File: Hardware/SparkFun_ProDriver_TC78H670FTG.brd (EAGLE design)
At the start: 50.8 x 57.1 mm, 87 parts, among them J2 LATCH, J3 PTH, J4 LATCH, J5 LATCH, J6 PTH, J7 LATCH, J8 PTH, U1 TC78H670FTG

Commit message: layout almost done still need to add bstop for heatsink
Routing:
- net MODE3: track 0.00 -> 91.9 mm
- net 3.3V: track 0.00 -> 79.0 mm, vias 0 -> 8
- net MODE2: track 0.00 -> 78.8 mm
- net EN: track 0.00 -> 71.6 mm
- net MODE1: track 0.00 -> 67.8 mm
- net MODE0: track 0.00 -> 59.2 mm
- net STBY: track 0.00 -> 47.6 mm
- net VREF: track 0.00 -> 45.1 mm, vias 0 -> 2
- net VM: track 1.21 -> 24.9 mm
- net OSCM: track 0.00 -> 8.56 mm
- net N$1: track 0.00 -> 6.17 mm
- net N$4: track 0.00 -> 6.02 mm
- net N$2: track 0.00 -> 1.98 mm
- net N$5: track 0.00 -> 1.79 mm
- added copper zone on layer 2, net GND
- added copper zone on layer 1, net OUT_A+
- added copper zone on layer 1, net OUT_A-
- added copper zone on layer 1, net OUT_B+
- added copper zone on layer 1, net OUT_B-
- removed copper zone on layer 2, net VM

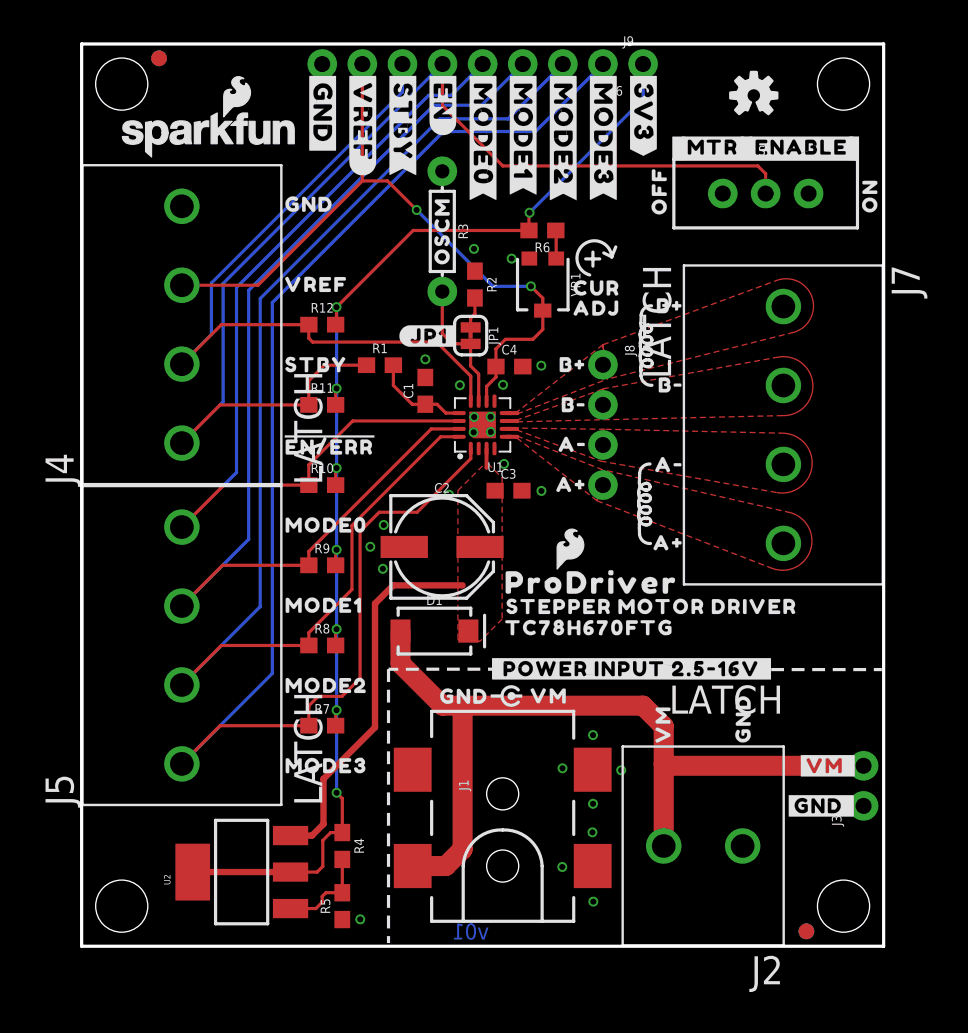
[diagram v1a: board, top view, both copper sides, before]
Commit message: nudged OSCM res away, added bstop for heatsink
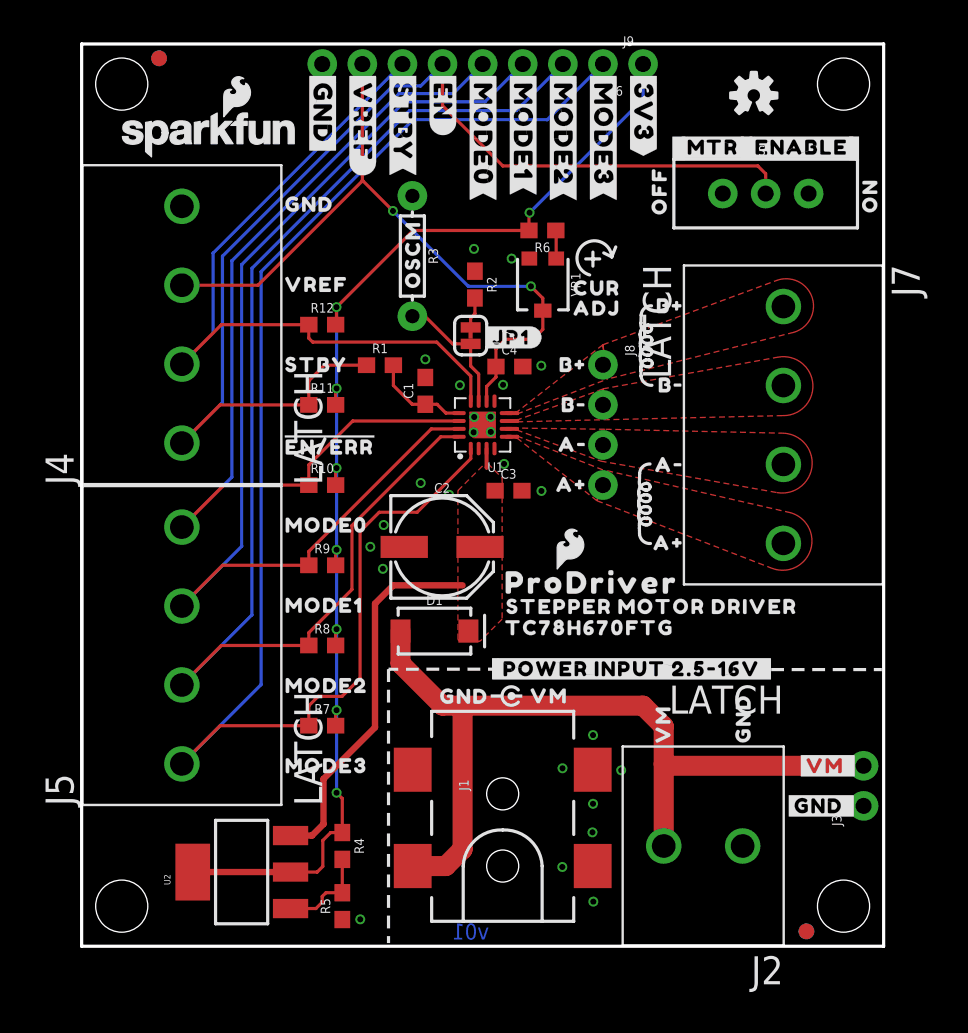
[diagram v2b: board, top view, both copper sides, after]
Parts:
- removed U$13: (no value), output:#JP1#0
- added U$45: (no value), output:#JP1#0
- moved R3 2.45 mm to (20.9, 43.7)
- moved U$18 2.39 mm to (21.0, 41.0)
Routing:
- net MODE3: track 91.9 -> 93.5 mm
- net MODE2: track 78.8 -> 80.2 mm
- net MODE1: track 67.8 -> 69.0 mm
- net MODE0: track 59.2 -> 60.3 mm
- net EN: track 71.6 -> 72.7 mm

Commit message: Corrected EN/ERR pin access
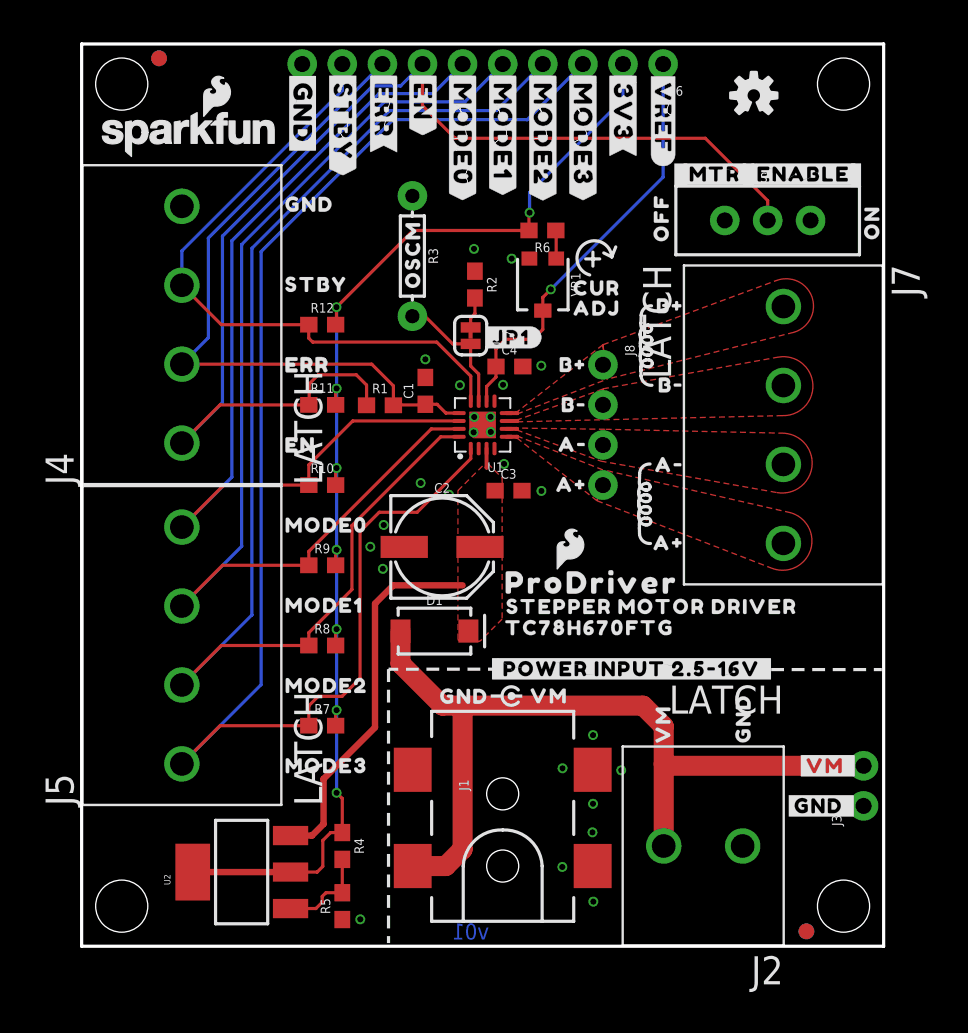
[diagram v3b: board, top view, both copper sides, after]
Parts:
- removed J9: (no value), SparkFun-Connectors:1X01_NO_SILK
- removed U$37: (no value), output:#MODE2#0
- removed U$38: (no value), output:#MODE3#0
- removed U$39: (no value), output:#3V3#0
- added U$13: (no value), output:#EN#2
- added U$46: (no value), output:#MODE1#4
- added U$47: (no value), output:#MODE2#4
- added U$48: (no value), output:#MODE3#4
- J6: device SparkFun-Connectors:1X08_NO_SILK -> SparkFun-Connectors:1X10_NO_SILK
- U$19: device output:#EN#ERR#0 -> output:EN0
- U$33: device output:#STBY#0 -> output:#MODE0#4
- U$34: device output:#EN#0 -> output:#STBY#3
- U$35: device output:#MODE0#0 -> output:#3V3#4
- U$36: device output:#MODE1#0 -> output:ERR4
- U$7: device output:VREF7 -> output:#ERR#7
- moved U$36 24.5 mm to (12.2, 36.8), turned to 0 degrees
- moved U$32 19.0 mm to (36.8, 55.5)
- moved U$7 15.3 mm to (19.1, 55.5), turned to 270 degrees
- moved U$35 8.86 mm to (34.3, 55.5)
- moved U$34 6.35 mm to (16.5, 55.5)
- moved U$8 5.08 mm to (12.2, 41.9)
- moved J6 3.81 mm to (36.8, 55.9)
- moved U$33 3.78 mm to (24.1, 55.5)
- moved R1 2.54 mm to (18.9, 34.3)
- moved S1 1.71 mm to (43.5, 46.0)
- moved U$17 1.71 mm to (36.7, 43.9)
- moved U$14 1.71 mm to (37.8, 48.9)
- moved U$16 1.71 mm to (50.1, 44.1)
- moved U$21 1.71 mm to (42.1, 48.9)
- moved LOGO1 1.27 mm to (6.84, 51.4)
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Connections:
- removed net N$1: C1.1, R1.2, U1.13
- new net ERR: C1.1, J4.2, J6.8, R1.2, U1.13
- net 3.3V: now also J6.2; no longer J9.1
- net EN: now also J6.7; no longer J6.5
- net GND: now also J6.10; no longer J6.8
- net MODE0: now also J6.6; no longer J6.4
- net MODE1: now also J6.5; no longer J6.3
- net MODE2: now also J6.4; no longer J6.2
- net MODE3: now also J6.3; no longer J6.1
- net STBY: now also J4.3, J6.9; no longer J4.2, J6.6
- net VREF: now also J6.1; no longer J4.3, J6.7
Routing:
- net ERR: track 0.00 -> 44.0 mm
- net VREF: track 45.1 -> 27.0 mm, vias 2 -> 1
- net STBY: track 47.6 -> 41.0 mm
- net N$1: track 6.17 -> 0.00 mm
- net EN: track 72.7 -> 75.5 mm
- net MODE3: track 93.5 -> 93.0 mm
- net MODE2: track 80.2 -> 79.7 mm
- net 3.3V: track 79.0 -> 78.5 mm
- net MODE1: track 69.0 -> 68.5 mm
- net MODE0: track 60.3 -> 59.8 mm

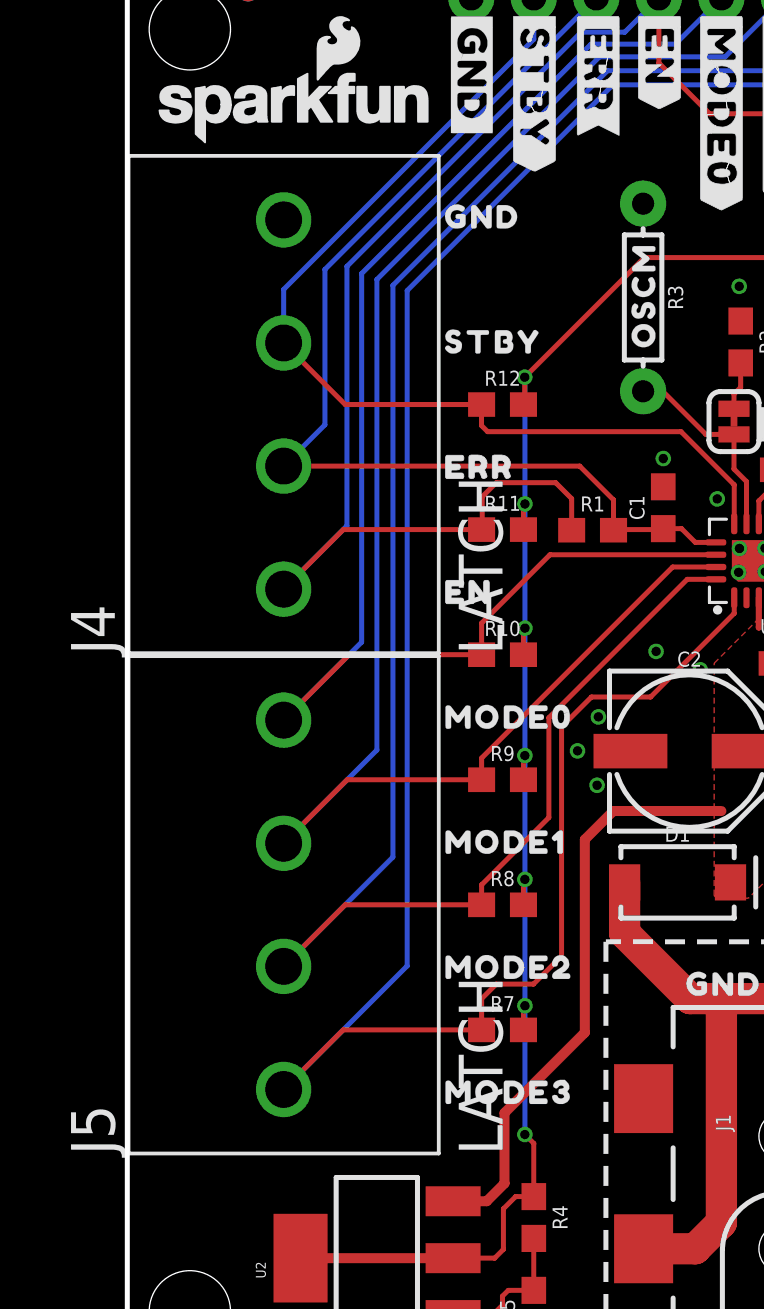
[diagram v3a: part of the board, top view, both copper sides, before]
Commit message: nudged 1x4 latch terminals apart to avoid part collision
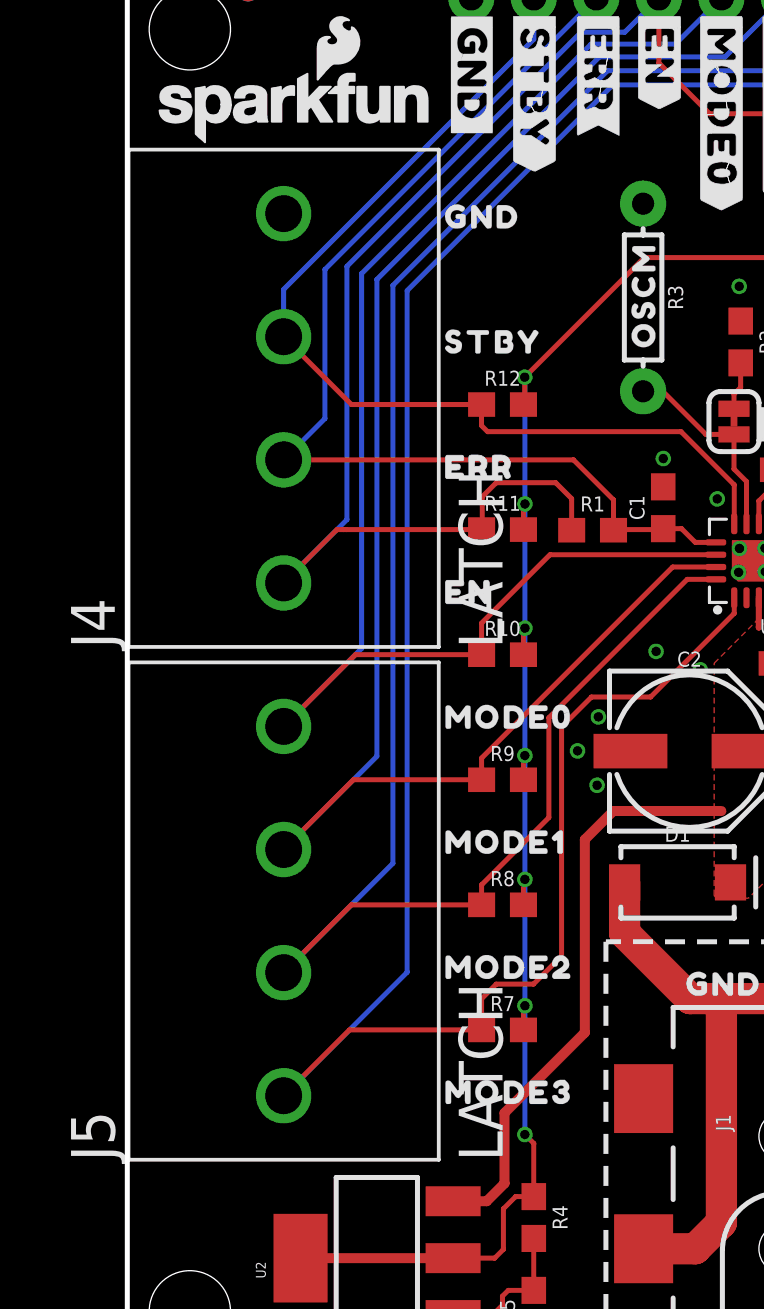
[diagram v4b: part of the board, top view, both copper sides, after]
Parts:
- moved J4 0.25 mm to (6.35, 39.6)
- moved J5 0.25 mm to (6.35, 18.8)

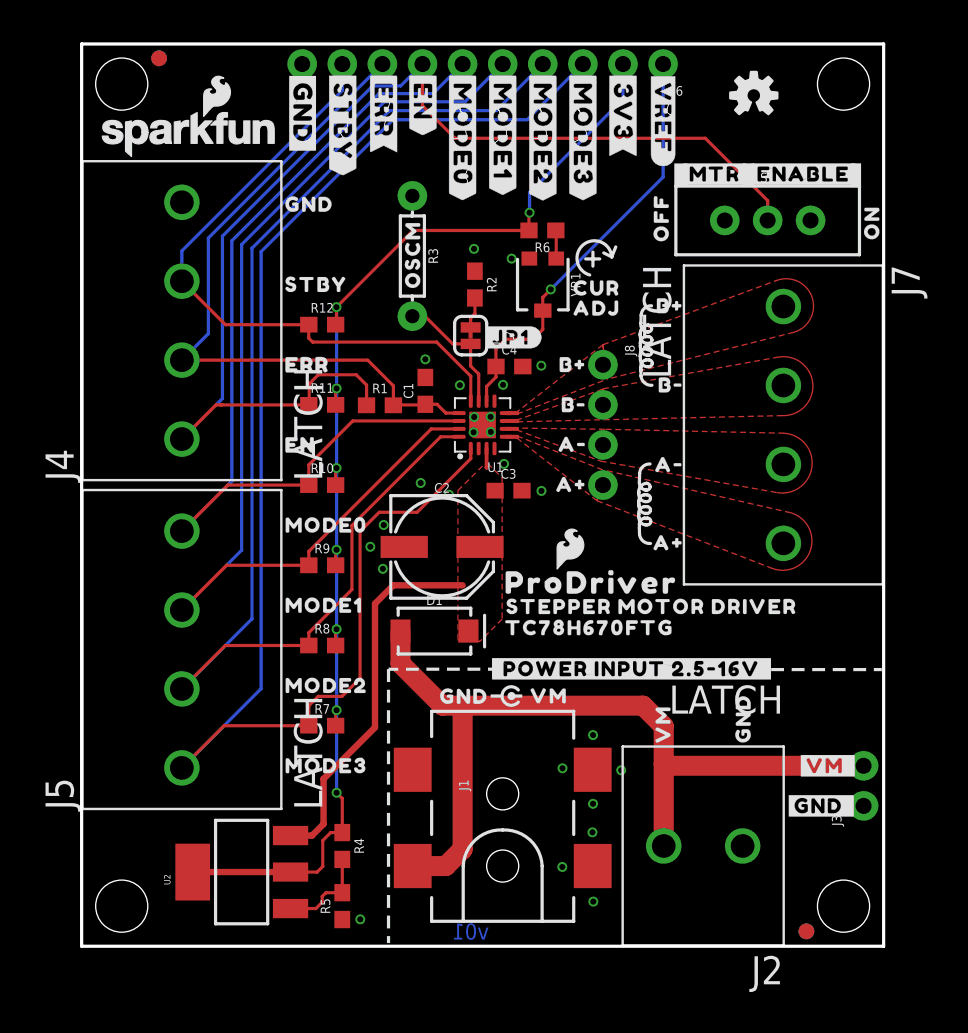
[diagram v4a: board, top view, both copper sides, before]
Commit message: moved connectors inward to allow for depanel blade space
Also added tcream to IC package
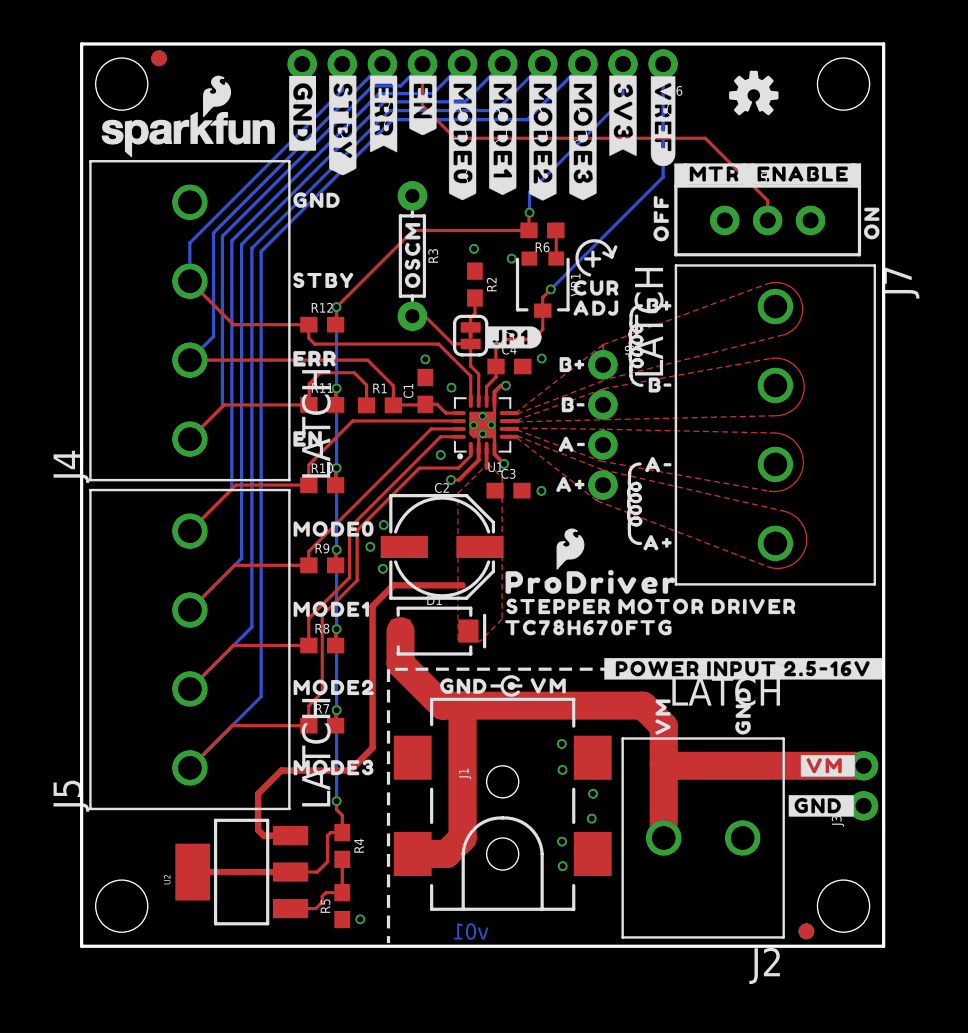
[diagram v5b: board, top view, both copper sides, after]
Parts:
- moved U$41 7.11 mm to (32.8, 17.6)
- moved J1 0.76 mm to (26.7, 5.84)
- moved U$29 0.63 mm to (22.0, 16.5)
- moved U$30 0.63 mm to (27.7, 16.5)
- moved U$19 0.63 mm to (12.7, 32.1)
- moved U$36 0.63 mm to (12.7, 37.2)
- moved U$1 0.63 mm to (38.2, 25.5)
- moved U$2 0.63 mm to (38.2, 35.5)
- moved U$3 0.63 mm to (38.2, 40.6)
- moved U$4 0.63 mm to (38.2, 30.5)
- moved U$8 0.57 mm to (12.7, 42.2)
- moved U$24 0.57 mm to (12.7, 21.3)
- moved U$26 0.57 mm to (12.7, 26.4)
- moved U$5 0.57 mm to (12.7, 47.2)
- moved U$25 0.52 mm to (12.7, 16.4)
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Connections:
- net N$3 renamed RAW
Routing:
- net GND: track 0.00 -> 10.4 mm, vias 25 -> 24
- net VM: track 24.9 -> 29.4 mm
- net MODE3: track 93.3 -> 91.8 mm
- net RAW: track 53.4 -> 52.1 mm
- net ERR: track 43.8 -> 43.0 mm
- net MODE2: track 80.0 -> 79.3 mm
- net MODE1: track 68.8 -> 68.1 mm
- net MODE0: track 60.1 -> 59.4 mm
- net STBY: track 40.8 -> 40.1 mm
- net EN: track 75.1 -> 74.5 mm
